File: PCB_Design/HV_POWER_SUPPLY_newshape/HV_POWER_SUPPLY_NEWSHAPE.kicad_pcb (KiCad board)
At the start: 4 copper layers, 57.3 x 57.3 mm, 80 parts, among them J1 Conn_01x02, J2 Conn_01x02, J3 Conn_01x02, J4 Conn_01x02, J5 Conn_01x02, Q2 DMN10H220L-7, U1 SN74LVC1G08DCKR_C5279048, U2 LTC1540IMS8#PBF, U3 LTC6906IS6#TRPBF, U4 LTC6994CS6-1-TRMPBF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

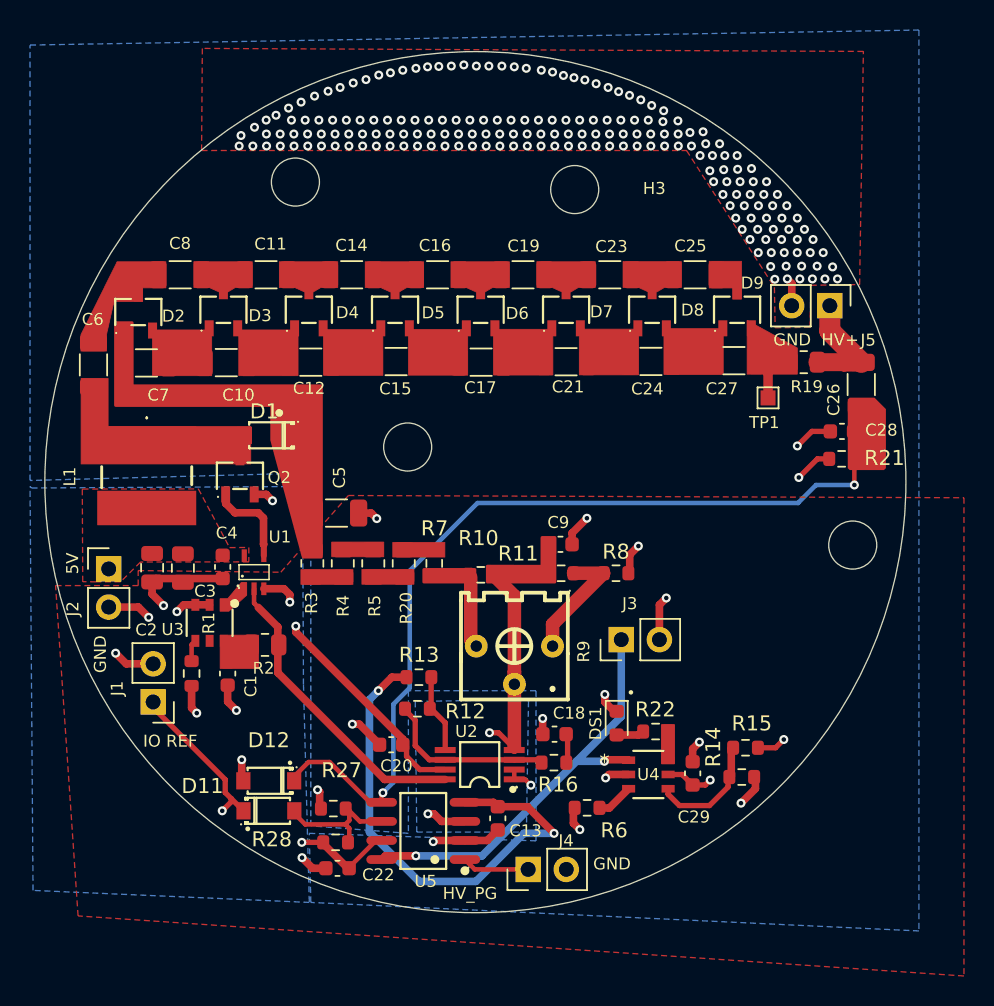
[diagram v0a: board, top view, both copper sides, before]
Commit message: -Zone clearance =.5 -added via for SYS_5V -adjust ground via
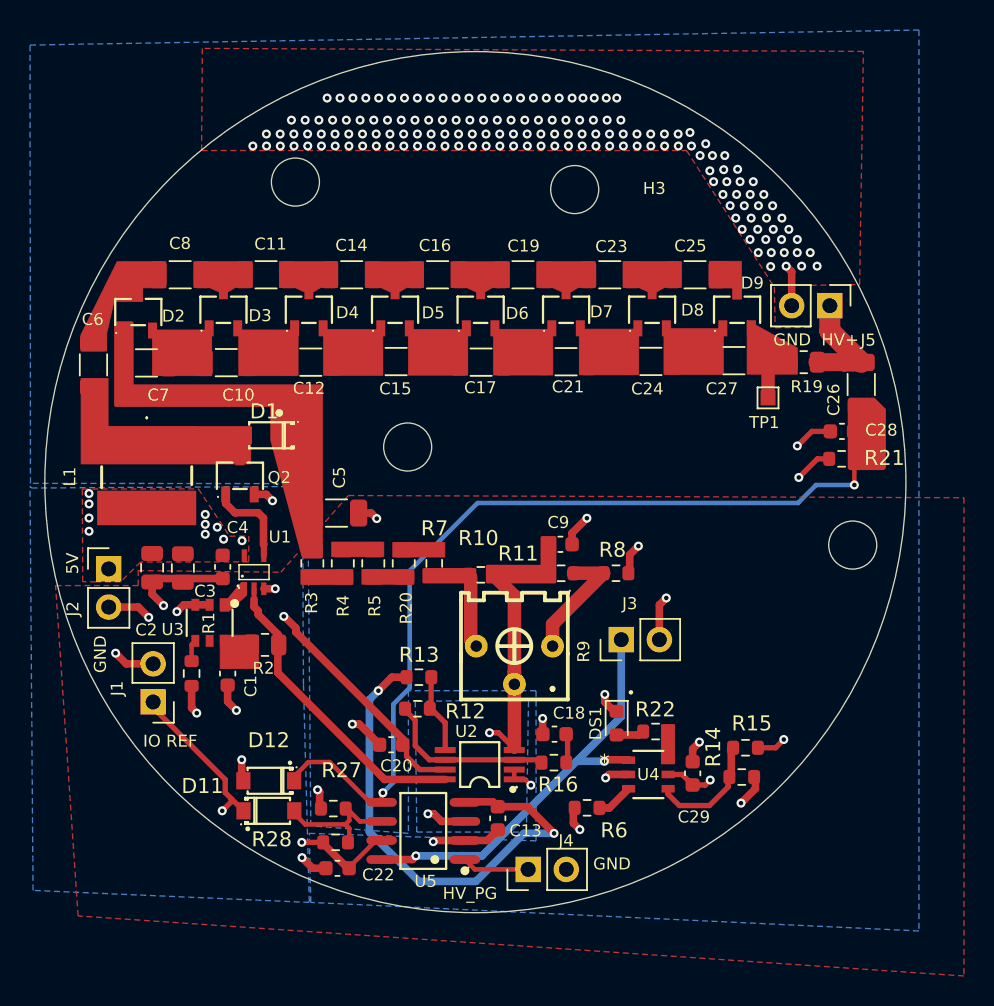
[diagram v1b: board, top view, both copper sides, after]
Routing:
- net SYS_5V: track 14.7 -> 15.7 mm, vias 1 -> 11
- net GND: track 55.9 -> 55.2 mm, vias 213 -> 178
